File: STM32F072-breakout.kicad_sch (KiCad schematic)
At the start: 29 parts, among them J1 USB_B_Micro, J2 Conn_01x04_Pin, J3 Conn_01x20_Pin, J4 Conn_01x20_Pin, SW1 SW_SPST, U1 STM32F072RBTx, U2 XC6206P332MR, Y1 8MHz

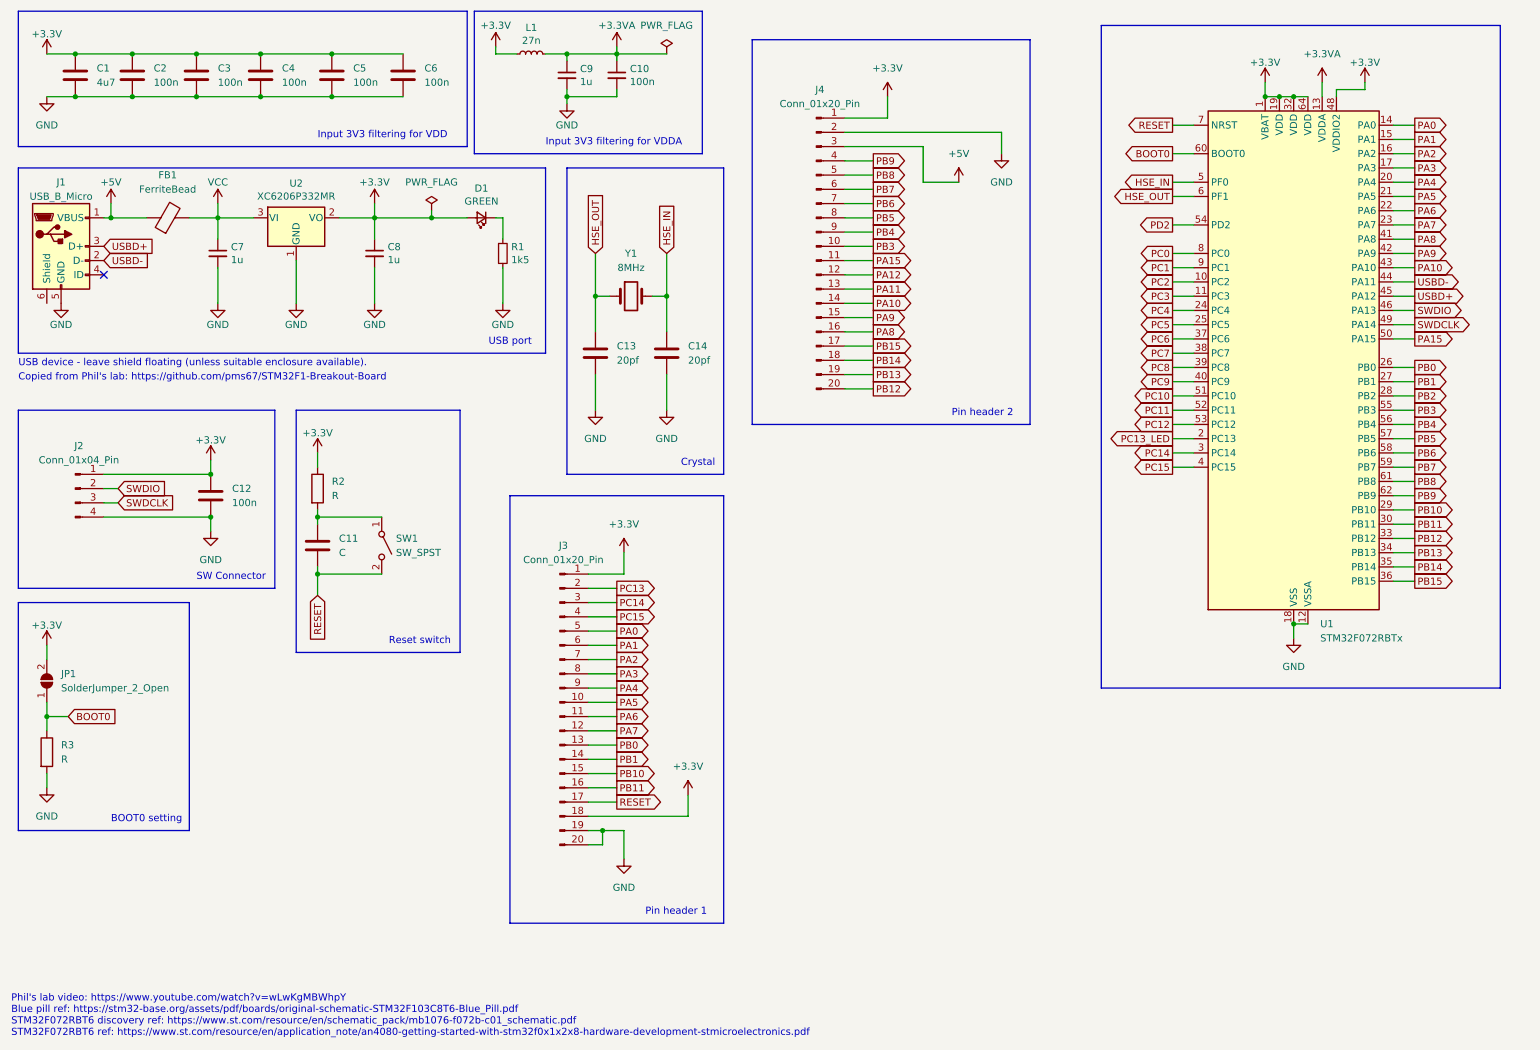
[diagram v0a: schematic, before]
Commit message: add one more header
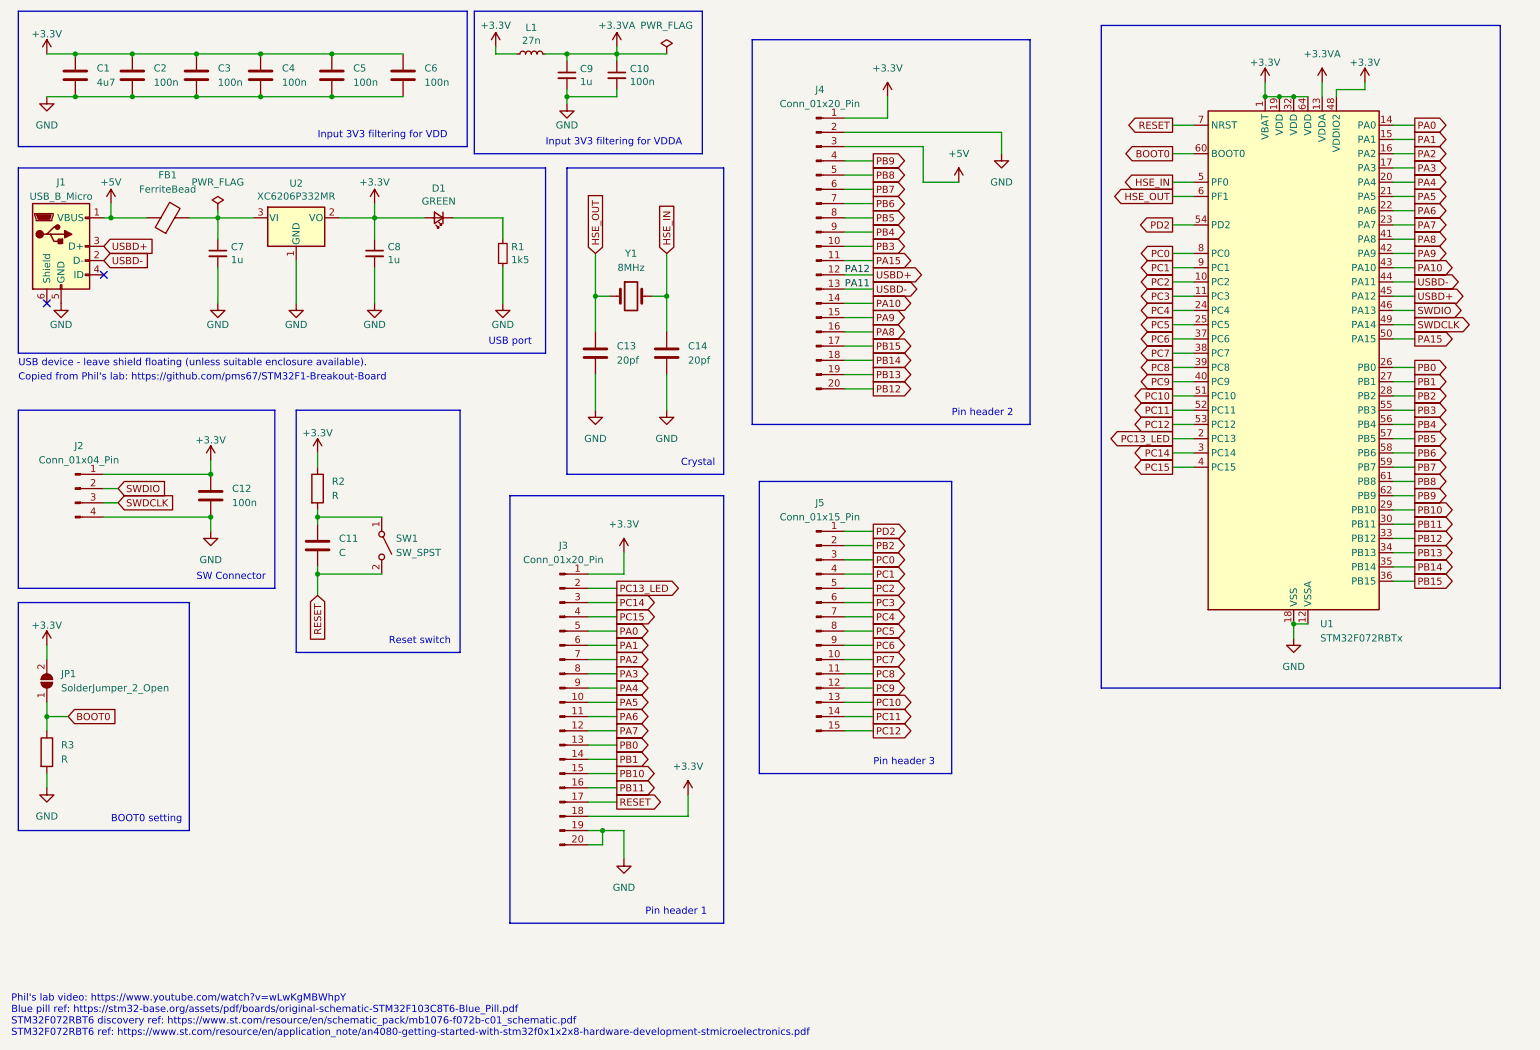
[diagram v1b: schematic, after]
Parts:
- added J5: Conn_01x15_Pin, Connector_PinHeader_1.00mm:PinHeader_1x15_P1.00mm_Vertical, symbol Connector:Conn_01x15_Pin
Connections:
- net PA11 is gone; now on net USBD-: J4.13 (Pin_13)
- net PA12 is gone; now on net USBD+: J4.12 (Pin_12)
- net PC13 is gone; now on net PC13_LED: J3.2 (Pin_2)
- net PB2: now also J5.2 (Pin_2)
- net PC0: now also J5.3 (Pin_3)
- net PC1: now also J5.4 (Pin_4)
- net PC10: now also J5.13 (Pin_13)
- net PC11: now also J5.14 (Pin_14)
- net PC12: now also J5.15 (Pin_15)
- net PC2: now also J5.5 (Pin_5)
- net PC3: now also J5.6 (Pin_6)
- net PC4: now also J5.7 (Pin_7)
- net PC5: now also J5.8 (Pin_8)
- net PC6: now also J5.9 (Pin_9)
- net PC7: now also J5.10 (Pin_10)
- net PC8: now also J5.11 (Pin_11)
- net PC9: now also J5.12 (Pin_12)
- net PD2: now also J5.1 (Pin_1)
- net VCC: no longer names the net of C7.1, FB1.2, U2.3 (VI)
- no-connect marks 1 -> 2
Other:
- note added: "Pin header 3"
- moved on the sheet: D1

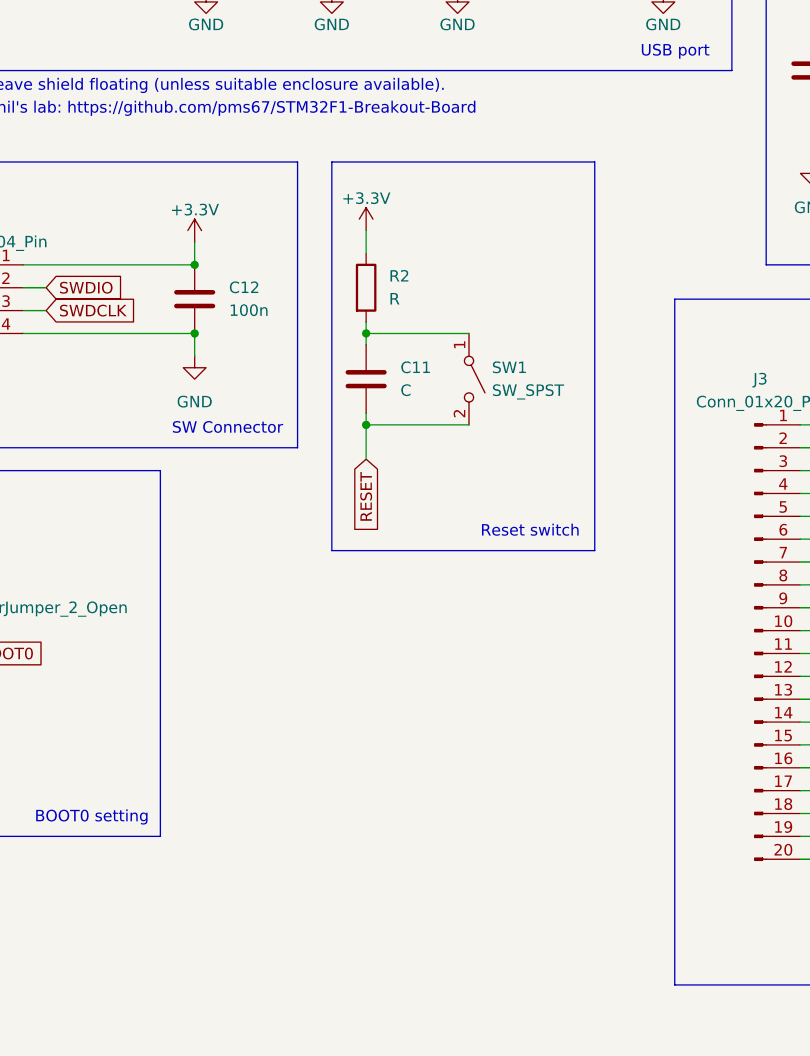
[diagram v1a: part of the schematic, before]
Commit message: add user LED
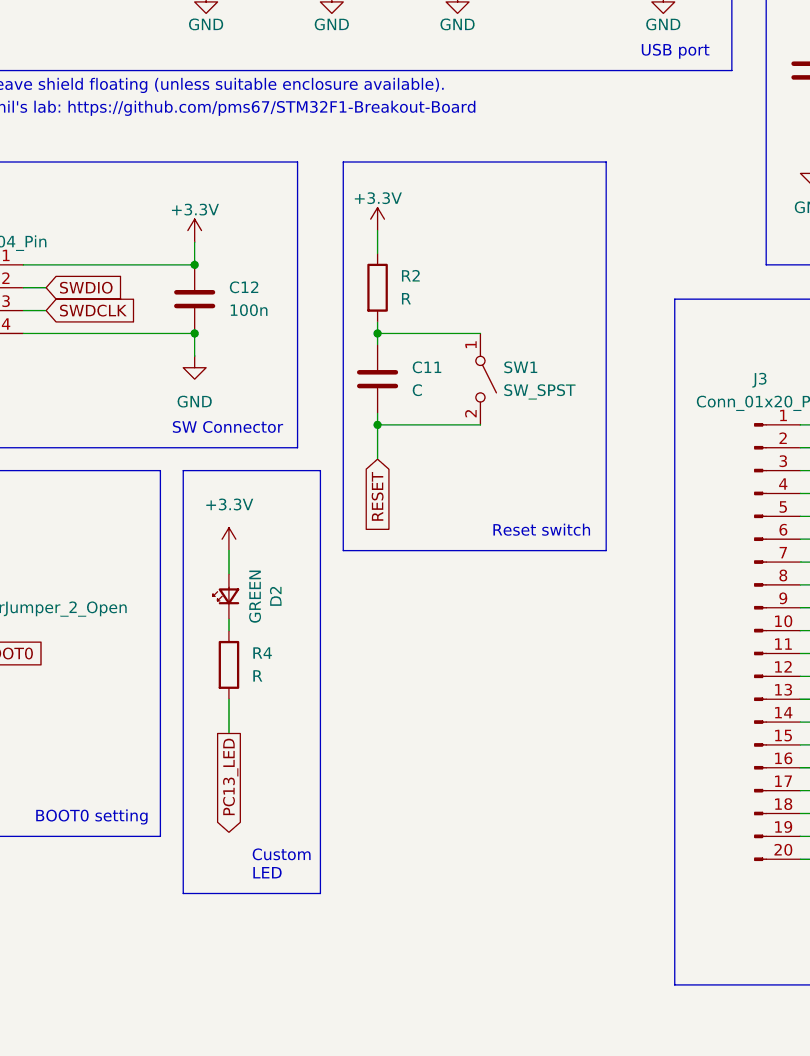
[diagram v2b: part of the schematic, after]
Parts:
- added D2: GREEN, LED_SMD:LED_0603_1608Metric, symbol Device:LED_Small
- added R4: R, symbol Device:R
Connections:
- net +3.3V: now also D2.2 (A)
- net PC13_LED: now also R4.2
- new net: D2.1 (K), R4.1
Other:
- note added: "Custom LED"
- moved on the sheet: C11, R2, SW1

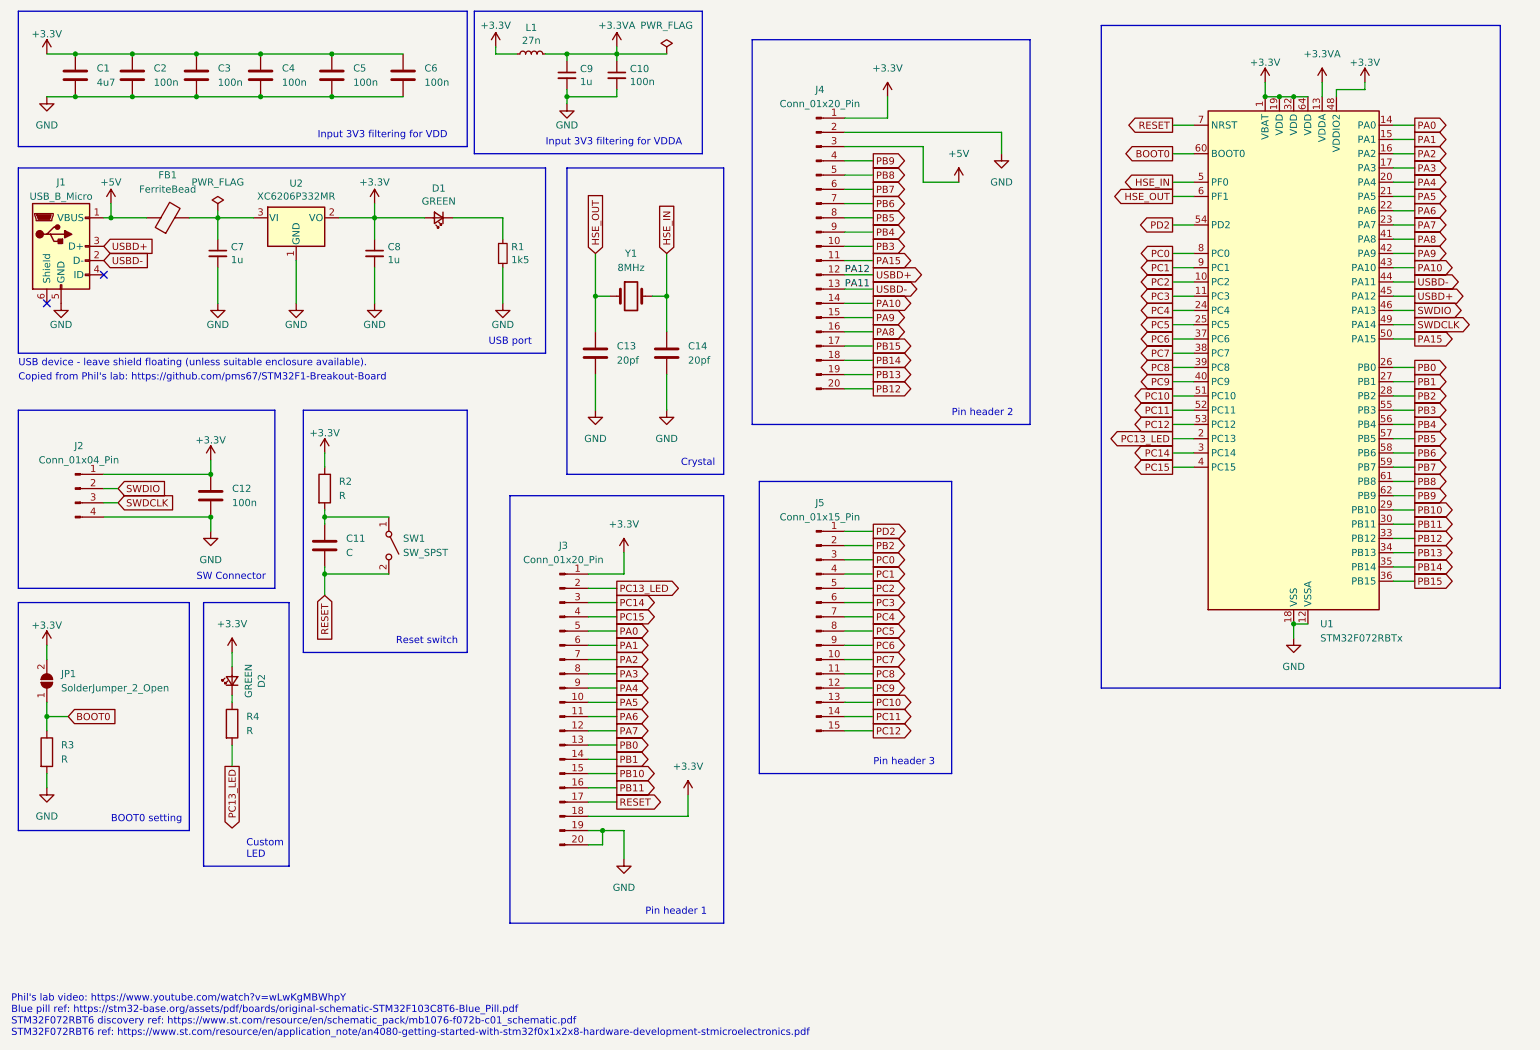
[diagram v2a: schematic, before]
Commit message: make same size headers
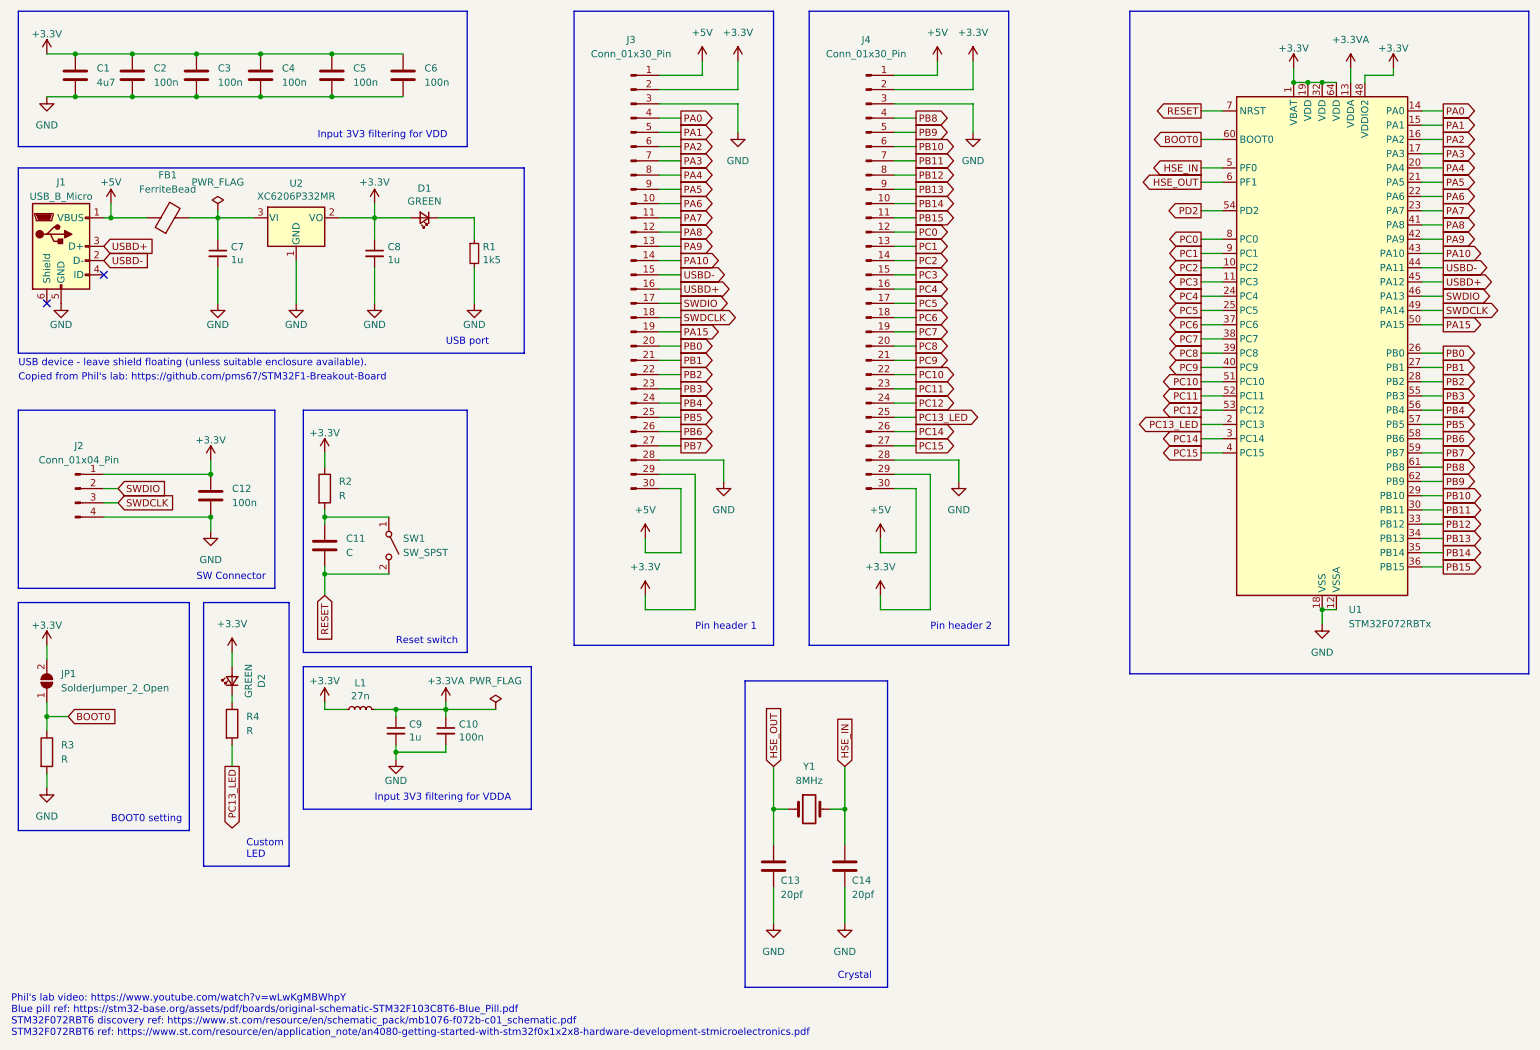
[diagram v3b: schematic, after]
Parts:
- removed J3: Conn_01x20_Pin, Connector_Molex:Molex_SL_171971-0020_1x20_P2.54mm_Vertical, symbol Connector:Conn_01x20_Pin
- removed J4: Conn_01x20_Pin, symbol Connector:Conn_01x20_Pin
- removed J5: Conn_01x15_Pin, Connector_PinHeader_1.00mm:PinHeader_1x15_P1.00mm_Vertical, symbol Connector:Conn_01x15_Pin
- added J3, J4: Conn_01x30_Pin, Connector_PinHeader_1.00mm:PinHeader_1x30_P1.00mm_Vertical, symbol Connector:Conn_01x30_Pin
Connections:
- net +3.3V: now also J3.2 (Pin_2), J3.29 (Pin_29), J4.2 (Pin_2), J4.29 (Pin_29)
- net +5V: now also J3.1 (Pin_1), J3.30 (Pin_30), J4.1 (Pin_1), J4.30 (Pin_30)
- net GND: now also J3.28 (Pin_28), J3.3 (Pin_3), J4.28 (Pin_28), J4.3 (Pin_3)
- net PA0: now also J3.4 (Pin_4)
- net PA1: now also J3.5 (Pin_5)
- net PA10: now also J3.14 (Pin_14)
- net PA15: now also J3.19 (Pin_19)
- net PA2: now also J3.6 (Pin_6)
- net PA3: now also J3.7 (Pin_7)
- net PA4: now also J3.8 (Pin_8)
- net PA5: now also J3.9 (Pin_9)
- net PA6: now also J3.10 (Pin_10)
- net PA7: now also J3.11 (Pin_11)
- net PA8: now also J3.12 (Pin_12)
- net PA9: now also J3.13 (Pin_13)
- net PB0: now also J3.20 (Pin_20)
- net PB1: now also J3.21 (Pin_21)
- net PB10: now also J4.6 (Pin_6)
- net PB11: now also J4.7 (Pin_7)
- net PB12: now also J4.8 (Pin_8)
- net PB13: now also J4.9 (Pin_9)
- net PB14: now also J4.10 (Pin_10)
- net PB15: now also J4.11 (Pin_11)
- net PB2: now also J3.22 (Pin_22)
- net PB3: now also J3.23 (Pin_23)
- net PB4: now also J3.24 (Pin_24)
- net PB5: now also J3.25 (Pin_25)
- net PB6: now also J3.26 (Pin_26)
- net PB7: now also J3.27 (Pin_27)
- net PB8: now also J4.4 (Pin_4)
- net PB9: now also J4.5 (Pin_5)
- net PC0: now also J4.12 (Pin_12)
- net PC1: now also J4.13 (Pin_13)
- net PC10: now also J4.22 (Pin_22)
- net PC11: now also J4.23 (Pin_23)
- net PC12: now also J4.24 (Pin_24)
- net PC13_LED: now also J4.25 (Pin_25)
- net PC14: now also J4.26 (Pin_26)
- net PC15: now also J4.27 (Pin_27)
- net PC2: now also J4.14 (Pin_14)
- net PC3: now also J4.15 (Pin_15)
- net PC4: now also J4.16 (Pin_16)
- net PC5: now also J4.17 (Pin_17)
- net PC6: now also J4.18 (Pin_18)
- net PC7: now also J4.19 (Pin_19)
- net PC8: now also J4.20 (Pin_20)
- net PC9: now also J4.21 (Pin_21)
- net SWDCLK: now also J3.18 (Pin_18)
- net SWDIO: now also J3.17 (Pin_17)
- net USBD+: now also J3.16 (Pin_16)
- net USBD-: now also J3.15 (Pin_15)
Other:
- note removed: "Pin header 3"
- moved on the sheet: C10, C13, C14, C9, D1, L1, R1, U1, Y1
